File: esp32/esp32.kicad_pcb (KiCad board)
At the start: 2 copper layers, 80 x 54 mm, 56 parts, among them IC1 KF33BDT-TR, J1 USB_C, J4 Conn_01x28, J5 Conn_01x28, Q1 FDN306P, Q2 FDS9926A, Q3 BC817, Q4 BC817, SW1 ON-OFF, SW2 Reset, SW3 Boot, U1 AP5056, U2 CP2102, U3 DW01A

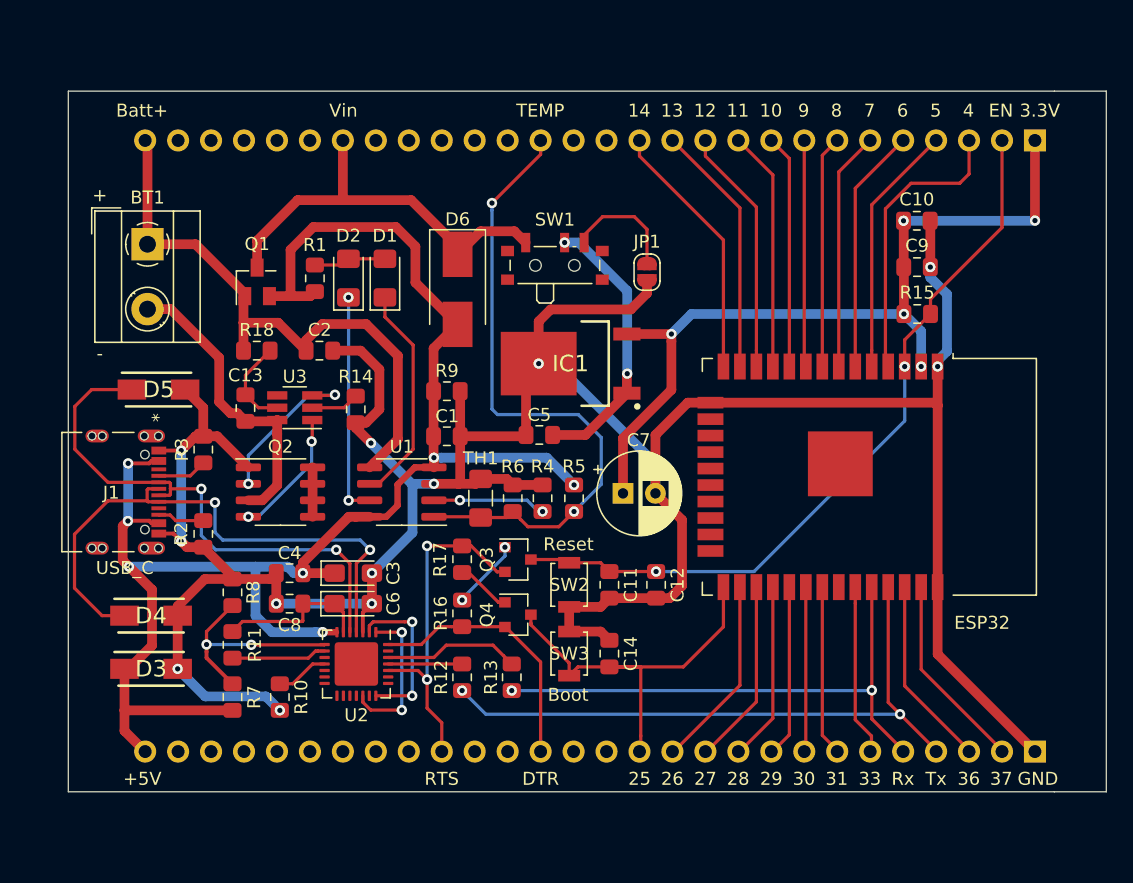
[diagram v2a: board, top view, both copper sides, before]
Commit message: Cambio de componentes: 1) USB-to-UART (CH340G por CP2102) 2) Dual Mosfet (8205A por FDS9926A)
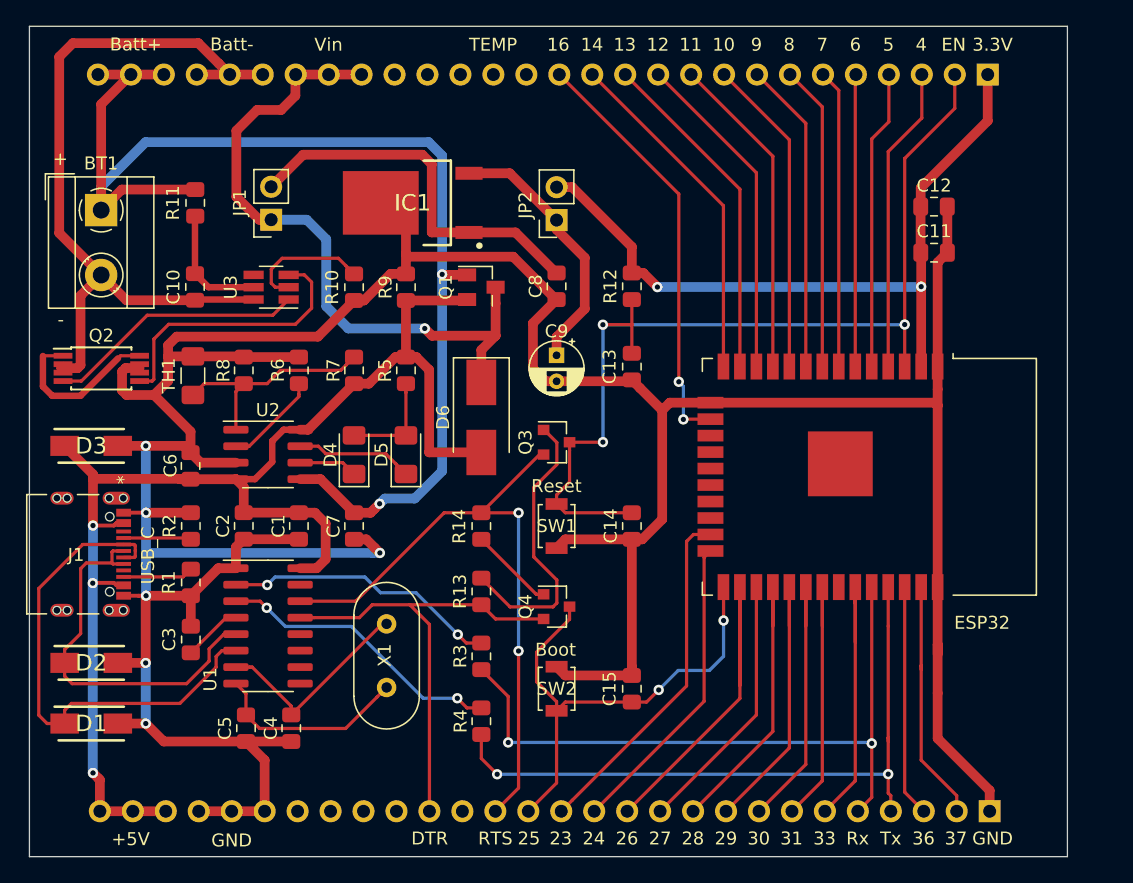
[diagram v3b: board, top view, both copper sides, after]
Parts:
- removed J4, J5: Conn_01x28, Connector_PinHeader_2.54mm:PinHeader_1x28_P2.54mm_Vertical
- removed R15, R16, R17: 10k, Resistor_SMD:R_0805_2012Metric_Pad1.15x1.40mm_HandSolder
- removed R18: 100, Resistor_SMD:R_0805_2012Metric_Pad1.15x1.40mm_HandSolder
- removed SW3: Boot, Button_Switch_SMD:SW_SPST_B3U-1000P
- added C15: 0.1uF, Capacitor_SMD:C_0805_2012Metric_Pad1.15x1.40mm_HandSolder, F.Cu at (134.4, 130.1)
- added J2: Conn_01x28, Connector_PinHeader_2.54mm:PinHeader_1x28_P2.54mm_Vertical, B.Cu at (161.9, 82.7)
- added J3: Conn_01x28, Connector_PinHeader_2.54mm:PinHeader_1x28_P2.54mm_Vertical, B.Cu at (162.0, 139.5)
- added JP2: Jumper_NO, Connector_PinSocket_2.54mm:PinSocket_1x02_P2.54mm_Vertical, F.Cu at (128.6, 93.9)
- added X1: 12 MHz, Crystal:Crystal_HC18-U_Vertical, F.Cu at (115.5, 125.1)
- C1: value 10uF -> 10u
- C10: value 10uF -> 0.1uF
- C11: value 1uF -> 10u
- C12: value 0.1uF -> 0.1u
- C13: value 0.1uF -> 1u
- C2: value 10uF -> 0.1u
- C3: value 4.7uF -> 0.1u; footprint Capacitor_Tantalum_SMD:CP_EIA-3216-12_Kemet-S_Pad1.58x1.35mm_HandSolder -> Capacitor_SMD:C_0805_2012Metric_Pad1.15x1.40mm_HandSolder
- C4: value 0.1uF -> 22p
- C5: value 1uF -> 22p
- C6: value 4.7uF -> 10uF; footprint Capacitor_Tantalum_SMD:CP_EIA-3216-12_Kemet-S_Pad1.58x1.35mm_HandSolder -> Capacitor_SMD:C_0805_2012Metric_Pad1.15x1.40mm_HandSolder
- C7: footprint Capacitor_THT:CP_Radial_D6.3mm_P2.50mm -> Capacitor_SMD:C_0805_2012Metric_Pad1.15x1.40mm_HandSolder
- C8: value 0.1uF -> 1uF
- C9: value 0.1uF -> 10uF; footprint Capacitor_SMD:C_0805_2012Metric_Pad1.15x1.40mm_HandSolder -> Capacitor_THT:CP_Radial_D4.0mm_P2.00mm
- D1: value GREEN -> SMAJ5.0A; footprint LED_SMD:LED_1206_3216Metric_Pad1.42x1.75mm_HandSolder -> SMAJ5.0A:DIOM5026X229N
- D2: value RED -> SMAJ5.0A; footprint LED_SMD:LED_1206_3216Metric_Pad1.42x1.75mm_HandSolder -> SMAJ5.0A:DIOM5026X229N
- D4: value SMAJ5.0A -> GREEN; footprint SMAJ5.0A:DIOM5026X229N -> LED_SMD:LED_1206_3216Metric_Pad1.42x1.75mm_HandSolder
- D5: value SMAJ5.0A -> RED; footprint SMAJ5.0A:DIOM5026X229N -> LED_SMD:LED_1206_3216Metric_Pad1.42x1.75mm_HandSolder
- JP1: footprint Jumper:SolderJumper-2_P1.3mm_Open_RoundedPad1.0x1.5mm -> Connector_PinSocket_2.54mm:PinSocket_1x02_P2.54mm_Vertical
- Q2: value FDS9926A -> 8205A; footprint Package_SO:SOIC-8_3.9x4.9mm_P1.27mm -> Package_SO:TSSOP-8_4.4x3mm_P0.65mm
- R1: value 1k -> 5.1k
- R10: value 10k -> 1k
- R11: value 4.7k -> 100
- R12, R13: value 100 -> 10k
- R14: value 1k -> 10k
- R3: value 5.1k -> 100
- R4: value 1k -> 100
- R5: value RT1 -> 1k
- R6: value RT2 -> 1k
- R7: value 22.1k -> RT1
- R8: value 47.5k -> RT2
- SW1: value ON-OFF -> Reset; footprint Button_Switch_SMD:SW_SPDT_PCM12 -> Button_Switch_SMD:SW_SPST_B3U-1000P
- SW2: value Reset -> Boot
- U1: value AP5056 -> CH340G; footprint Package_SO:SOIC-8_3.9x4.9mm_P1.27mm -> Package_SO:SOIC-16_3.9x9.9mm_P1.27mm
- U2: value CP2102 -> AP5056; footprint Package_DFN_QFN:QFN-28-1EP_5x5mm_P0.5mm_EP3.35x3.35mm -> Package_SO:SOIC-8_3.9x4.9mm_P1.27mm
- moved C10 55.9 mm to (100.8, 99.1), turned to 270 degrees
- moved D1 41.1 mm to (92.8, 132.7), turned to 0 degrees
- moved C12 36.2 mm to (157.7, 92.9), turned to 180 degrees
- moved C11 35.8 mm to (157.7, 96.5), turned to 0 degrees
- moved D2 35.7 mm to (92.8, 128.1), turned to 0 degrees
- moved R11 34.2 mm to (100.8, 92.6), turned to 270 degrees
- moved R12 32.9 mm to (134.4, 99.0), turned to 270 degrees
- moved R10 32.1 mm to (113.0, 99.1)
- moved C5 32.0 mm to (104.7, 133.1), turned to 270 degrees
- moved C8 32.0 mm to (128.6, 99.0), turned to 270 degrees
- moved C13 30.0 mm to (134.4, 105.2)
- moved JP1 29.3 mm to (106.6, 93.9), turned to 180 degrees
- moved C9 28.6 mm to (128.6, 104.4), turned to 270 degrees
- moved R7 26.9 mm to (113.0, 105.5)
- moved R3 26.7 mm to (122.8, 127.6)
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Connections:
- BT1 pad 2: Net-(BT1-Pad2) -> Batt-
- C1 pad 2: Batt- -> GND
- C10 pad 1: +3V3 -> Net-(C10-Pad1)
- C11 pad 1: EN -> +3V3
- C11 pad 2: Batt- -> GND
- C12 pad 1: EN -> GND
- C12 pad 2: Batt- -> +3V3
- C13 pad 1: Net-(C13-Pad1) -> EN
- C13 pad 2: Net-(BT1-Pad2) -> GND
- C14 pad 1: Boot -> EN
- C14 pad 2: Batt- -> GND
- C2 pad 1: Batt+ -> VBUS
- C2 pad 2: Batt- -> GND
- C3 pad 1: VBUS -> Net-(C3-Pad1)
- C3 pad 2: Batt- -> GND
- C4 pad 1: VBUS -> Net-(C4-Pad1)
- C4 pad 2: Batt- -> GND
- C5 pad 2: Batt- -> GND
- C6 pad 1: Net-(C6-Pad1) -> VBUS
- C6 pad 2: Batt- -> GND
- C7 pad 1: +3V3 -> Batt+
- C7 pad 2: Batt- -> GND
- C8 pad 1: Net-(C6-Pad1) -> Net-(C8-Pad1)
- C8 pad 2: Batt- -> GND
- C9 pad 1: +3V3 -> Net-(C9-Pad1)
- C9 pad 2: Batt- -> GND
- D1 pad 1: Net-(D1-Pad1) -> D-
- D1 pad 2: Net-(D1-Pad2) -> GND
- D2 pad 1: Net-(D2-Pad1) -> D+
- D2 pad 2: Net-(D1-Pad2) -> GND
- D3 pad 2: Batt- -> GND
- D4 pad 2: Batt- -> Net-(D4-Pad2)
- D5 pad 2: Batt- -> Net-(D4-Pad2)
- ESP32 pad 1: Batt- -> GND
- ESP32 pad 15: Batt- -> GND
- ESP32 pad 38: Batt- -> GND
- IC1 pad 1: Net-(C5-Pad1) -> Net-(C8-Pad1)
- IC1 pad 3: +3V3 -> Net-(C9-Pad1)
- IC1 pad 4: Batt- -> GND
- J1 pad A1-B12: Batt- -> GND
- J1 pad A6: Net-(D4-Pad1) -> D+
- J1 pad A7: Net-(D5-Pad1) -> D-
- J1 pad B1-A12: Batt- -> GND
- J1 pad B6: Net-(D4-Pad1) -> D+
- J1 pad B7: Net-(D5-Pad1) -> D-
- JP1 pad 1: Net-(JP1-Pad1) -> Vin
- JP1 pad 2: Batt- -> Net-(C8-Pad1)
- Q2 pad 1: Batt- -> Net-(Q2-Pad1)
- Q2 pad 2: Net-(Q2-Pad2) -> Batt-
- Q2 pad 3: Net-(BT1-Pad2) -> Batt-
- Q2 pad 6: Net-(Q2-Pad5) -> GND
- Q2 pad 7: Net-(Q2-Pad5) -> GND
- Q2 pad 8: Net-(Q2-Pad5) -> Net-(Q2-Pad1)
- R1 pad 1: VBUS -> Net-(J1-PadB5)
- R1 pad 2: Net-(D1-Pad2) -> GND
- R10 pad 2: Batt- -> GND
- R11 pad 1: Net-(R11-Pad1) -> Batt+
- R11 pad 2: Net-(C6-Pad1) -> Net-(C10-Pad1)
- R12 pad 1: Tx -> +3V3
- R12 pad 2: Net-(R12-Pad2) -> EN
- R13 pad 1: Rx -> Net-(Q3-Pad1)
- R13 pad 2: Net-(R13-Pad2) -> DTR
- R14 pad 1: Net-(R14-Pad1) -> Net-(Q4-Pad1)
- R14 pad 2: Batt- -> RTS
- R2 pad 1: Net-(J1-PadB5) -> Net-(J1-PadA5)
- R2 pad 2: Batt- -> GND
- R3 pad 1: Net-(J1-PadA5) -> Rx
- R3 pad 2: Batt- -> Net-(R3-Pad2)
- R4 pad 1: Net-(R4-Pad1) -> Tx
- R4 pad 2: Batt- -> Net-(R4-Pad2)
- R5 pad 2: Temp -> Net-(D4-Pad2)
- R6 pad 1: Temp -> Net-(R6-Pad1)
- R6 pad 2: Batt- -> GND
- R7 pad 2: Net-(R7-Pad2) -> Temp
- R8 pad 1: Net-(R7-Pad2) -> Temp
- R8 pad 2: Batt- -> GND
- R9 pad 2: Batt- -> GND
- SW1 pad 1: Vin -> EN
- SW1 pad 2: Net-(C5-Pad1) -> GND
- SW2 pad 1: EN -> Boot
- SW2 pad 2: Batt- -> GND
- TH1 pad 2: Batt- -> GND
- U1 pad 1: Temp -> GND
- U1 pad 2: Net-(R4-Pad1) -> Net-(R3-Pad2)
- U1 pad 3: Batt- -> Net-(R4-Pad2)
- U1 pad 4: VBUS -> Net-(C3-Pad1)
- U1 pad 5: Batt+ -> D+
- U1 pad 6: Net-(D1-Pad1) -> D-
- U1 pad 7: Net-(D2-Pad1) -> Net-(C4-Pad1)
- U1 pad 8: VBUS -> Net-(C5-Pad1)
- U2 pad 1: Net-(U2-Pad1) -> Temp
- U2 pad 2: Net-(U2-Pad2) -> Net-(R6-Pad1)
- U2 pad 3: Batt- -> GND
- U2 pad 4: Net-(D4-Pad1) -> VBUS
- U2 pad 5: Net-(D5-Pad1) -> Batt+
- U2 pad 6: Net-(C6-Pad1) -> Net-(D4-Pad1)
- U2 pad 7: VBUS -> Net-(D5-Pad1)
- U2 pad 8: Net-(R7-Pad2) -> VBUS
- U3 pad 2: Net-(R14-Pad1) -> Net-(R10-Pad1)
- U3 pad 3: Net-(Q2-Pad2) -> Net-(Q2-Pad5)
- U3 pad 5: Net-(C13-Pad1) -> Net-(C10-Pad1)
- U3 pad 6: Net-(BT1-Pad2) -> Batt-
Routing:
- net GND: track 0.00 -> 309.6 mm, vias 0 -> 6
- net Batt-: track 264.2 -> 61.0 mm, vias 12 -> 0
- net Batt+: track 50.5 -> 93.9 mm, vias 0 -> 2
- net Net-(D4-Pad1): track 44.2 -> 4.52 mm, vias 2 -> 0
- net D-: track 0.00 -> 39.3 mm
- net Net-(D5-Pad1): track 42.1 -> 9.04 mm, vias 2 -> 0
- net Temp: track 50.1 -> 17.4 mm, vias 2 -> 0
- net 16: track 0.00 -> 32.6 mm, vias 0 -> 2
- net Net-(C8-Pad1): track 0.00 -> 29.8 mm
- net D+: track 0.00 -> 29.7 mm
- net 23: track 0.00 -> 26.9 mm
- net VBUS: track 131.2 -> 104.4 mm, vias 7 -> 3
- net 24: track 0.00 -> 23.8 mm
- net RTS: track 26.4 -> 50.1 mm
- net Net-(BT1-Pad2): track 23.4 -> 0.00 mm
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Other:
- board size 80 x 54 mm -> 80 x 64 mm
- net class Default: clearance 0.2 -> 0.25
- net class MID added: clearance 0.25, trace_width 0.5, via_dia 0.8, via_drill 0.4
- net class PWR: clearance 0.2 -> 0.25
- rule trace_clearance: 0.2 -> 0.25
- board text added: "16"
- board text added: "23"
- board text added: "24"
- board text added: "Batt-"

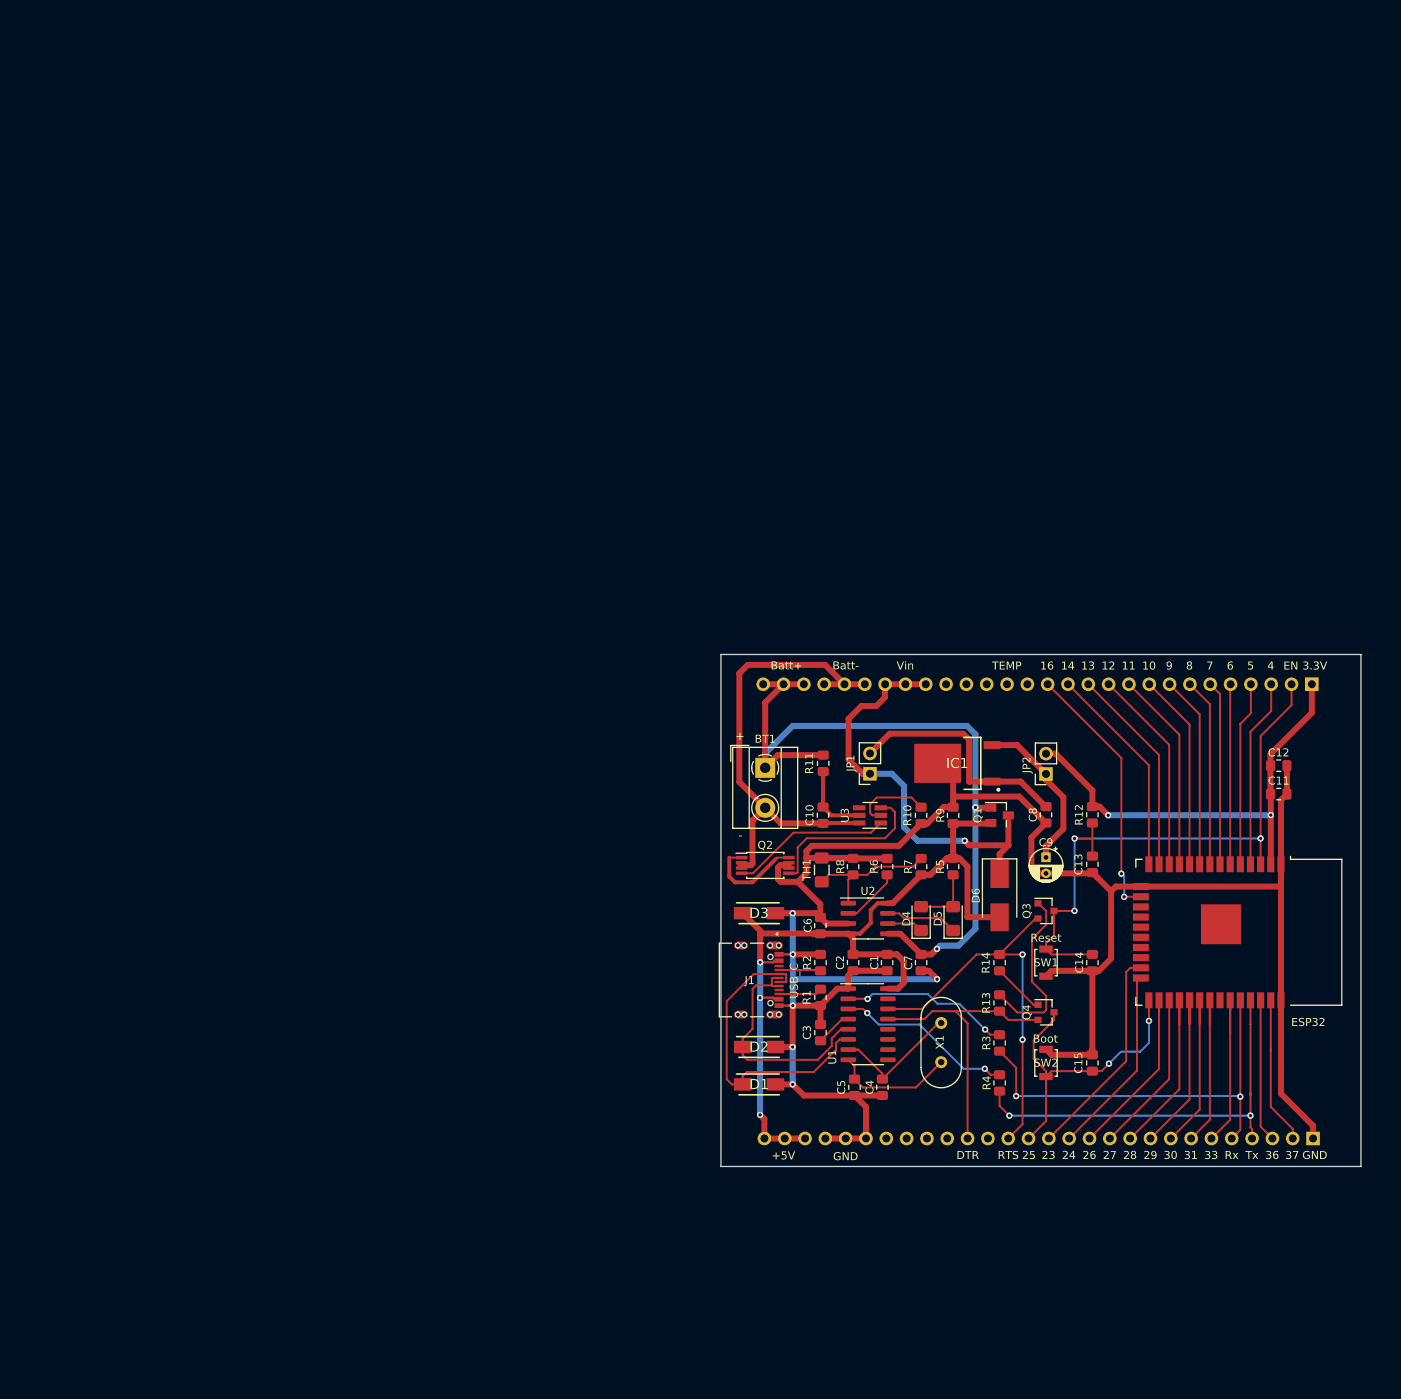
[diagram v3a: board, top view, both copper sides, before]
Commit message: 1) Medicion de bateria - 2) Agujeros para tornillos - 3) Nombre de integarntes y proyecto
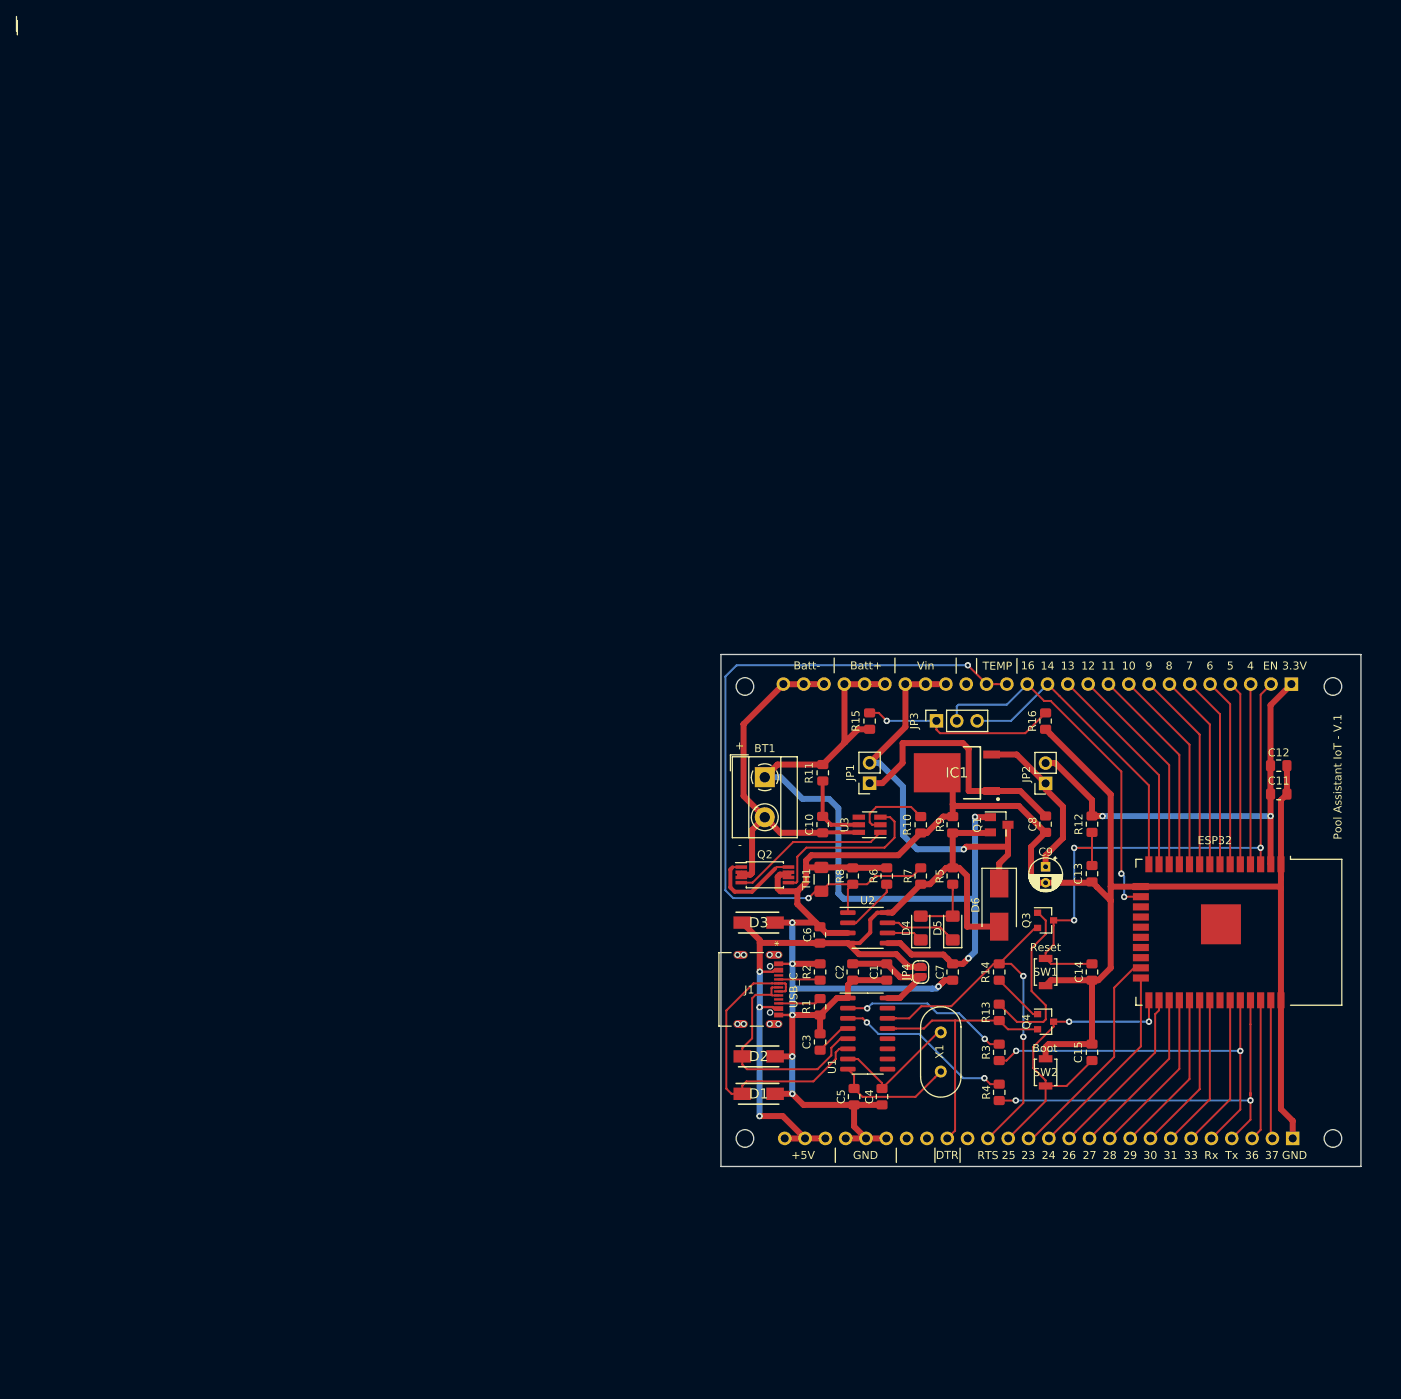
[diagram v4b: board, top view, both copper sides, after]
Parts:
- added G***: LOGO, FIUBA:FIUBA, B.Cu at (150.8, 93.3)
- added Hole1: MountingHole_2.2mm_M2_ISO7380, MountingHole:MountingHole_2.2mm_M2_ISO7380, F.Cu at (91.0, 83.0)
- added Hole2: MountingHole_2.2mm_M2_ISO7380, MountingHole:MountingHole_2.2mm_M2_ISO7380, F.Cu at (164.5, 83.0)
- added Hole3: MountingHole_2.2mm_M2_ISO7380, MountingHole:MountingHole_2.2mm_M2_ISO7380, F.Cu at (91.0, 139.5)
- added Hole4: MountingHole_2.2mm_M2_ISO7380, MountingHole:MountingHole_2.2mm_M2_ISO7380, F.Cu at (164.5, 139.5)
- added JP3: Jumper_3_Open, Connector_PinSocket_2.54mm:PinSocket_1x03_P2.54mm_Vertical, F.Cu at (114.9, 87.3)
- added JP4: SolderJumper_NO, Jumper:SolderJumper-2_P1.3mm_Open_RoundedPad1.0x1.5mm, F.Cu at (113.0, 118.7)
- added R15: 10k, Resistor_SMD:R_0805_2012Metric_Pad1.15x1.40mm_HandSolder, F.Cu at (106.6, 87.3)
- added R16: 22k, Resistor_SMD:R_0805_2012Metric_Pad1.15x1.40mm_HandSolder, F.Cu at (128.6, 87.3)
- J2, J3: value Conn_01x28 -> Conn_01x26; footprint Connector_PinHeader_2.54mm:PinHeader_1x28_P2.54mm_Vertical -> Connector_PinHeader_2.54mm:PinHeader_1x26_P2.54mm_Vertical
- moved C7 4.11 mm to (117.0, 118.7)
- moved J2 2.56 mm to (159.3, 82.7)
- moved J3 2.54 mm to (159.5, 139.5)
- moved C15 1.33 mm to (134.4, 128.7)
- moved C4 1.18 mm to (108.1, 134.3)
- moved C5 1.18 mm to (104.6, 134.3)
- moved D2 1.18 mm to (92.7, 129.2)
- moved R1 1.18 mm to (100.4, 123.0)
- moved R3 1.18 mm to (122.8, 128.7)
- moved R4 1.18 mm to (122.8, 133.7)
- moved SW2 1.18 mm to (128.6, 131.2)
- moved C10 1.18 mm to (100.7, 100.3)
- moved C13 1.18 mm to (134.4, 106.4)
- moved C14 1.18 mm to (134.4, 118.7)
- moved D3 1.18 mm to (92.7, 112.5)
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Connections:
- C1 pad 1: VBUS -> Net-(C1-Pad1)
- C2 pad 1: VBUS -> Net-(C1-Pad1)
- J2 pad 15: Net-(J2-Pad15) -> Temp
- J2 pad 18: Net-(J2-Pad18) -> Vin
- J2 pad 19: Net-(J2-Pad19) -> Vin
- J2 pad 21: Vin -> Batt+
- J2 pad 22: Vin -> Batt+
- J2 pad 23: Batt- -> Batt+
- J2 pad 26: Batt+ -> Batt-
- J3 pad 21: Net-(J3-Pad21) -> GND
- J3 pad 22: Net-(J3-Pad22) -> GND
- J3 pad 24: GND -> VBUS
- J3 pad 25: GND -> VBUS
- JP1 pad 1: Vin -> Net-(C8-Pad1)
- JP1 pad 2: Net-(C8-Pad1) -> Vin
- U1 pad 16: VBUS -> Net-(C1-Pad1)
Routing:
- net Temp: track 17.4 -> 93.7 mm, vias 0 -> 2
- net Net-(JP3-Pad1): track 0.00 -> 24.7 mm, vias 0 -> 1
- net GND: track 309.6 -> 329.8 mm
- net Net-(C1-Pad1): track 0.00 -> 14.4 mm
- net 16: track 32.6 -> 46.0 mm
- net Batt-: track 61.0 -> 48.1 mm
- net 14: track 26.7 -> 38.5 mm
- net 26: track 28.4 -> 21.9 mm
- net 33: track 23.7 -> 19.3 mm
- net Batt+: track 93.9 -> 98.2 mm
- net Rx: track 52.2 -> 49.4 mm
- net Vin: track 52.7 -> 50.0 mm
- net Net-(C8-Pad1): track 29.8 -> 32.4 mm
- net 30: track 21.8 -> 19.8 mm
- net 29: track 22.3 -> 20.3 mm
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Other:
- board text added: "Gonzalo Gilces Duran Rodrigo Nahuel Parra Segundo Molina Abeniacar"
- board text added: "Pool Assistant IoT - V.1"
